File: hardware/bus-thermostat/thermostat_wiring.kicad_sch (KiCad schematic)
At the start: 44 parts, among them Q1 2N7002, Q2 2N7002, Q3 2N7002, Q4 IRF540N, Q5 IRF540N, T1 1:2, U1 UCC27714D

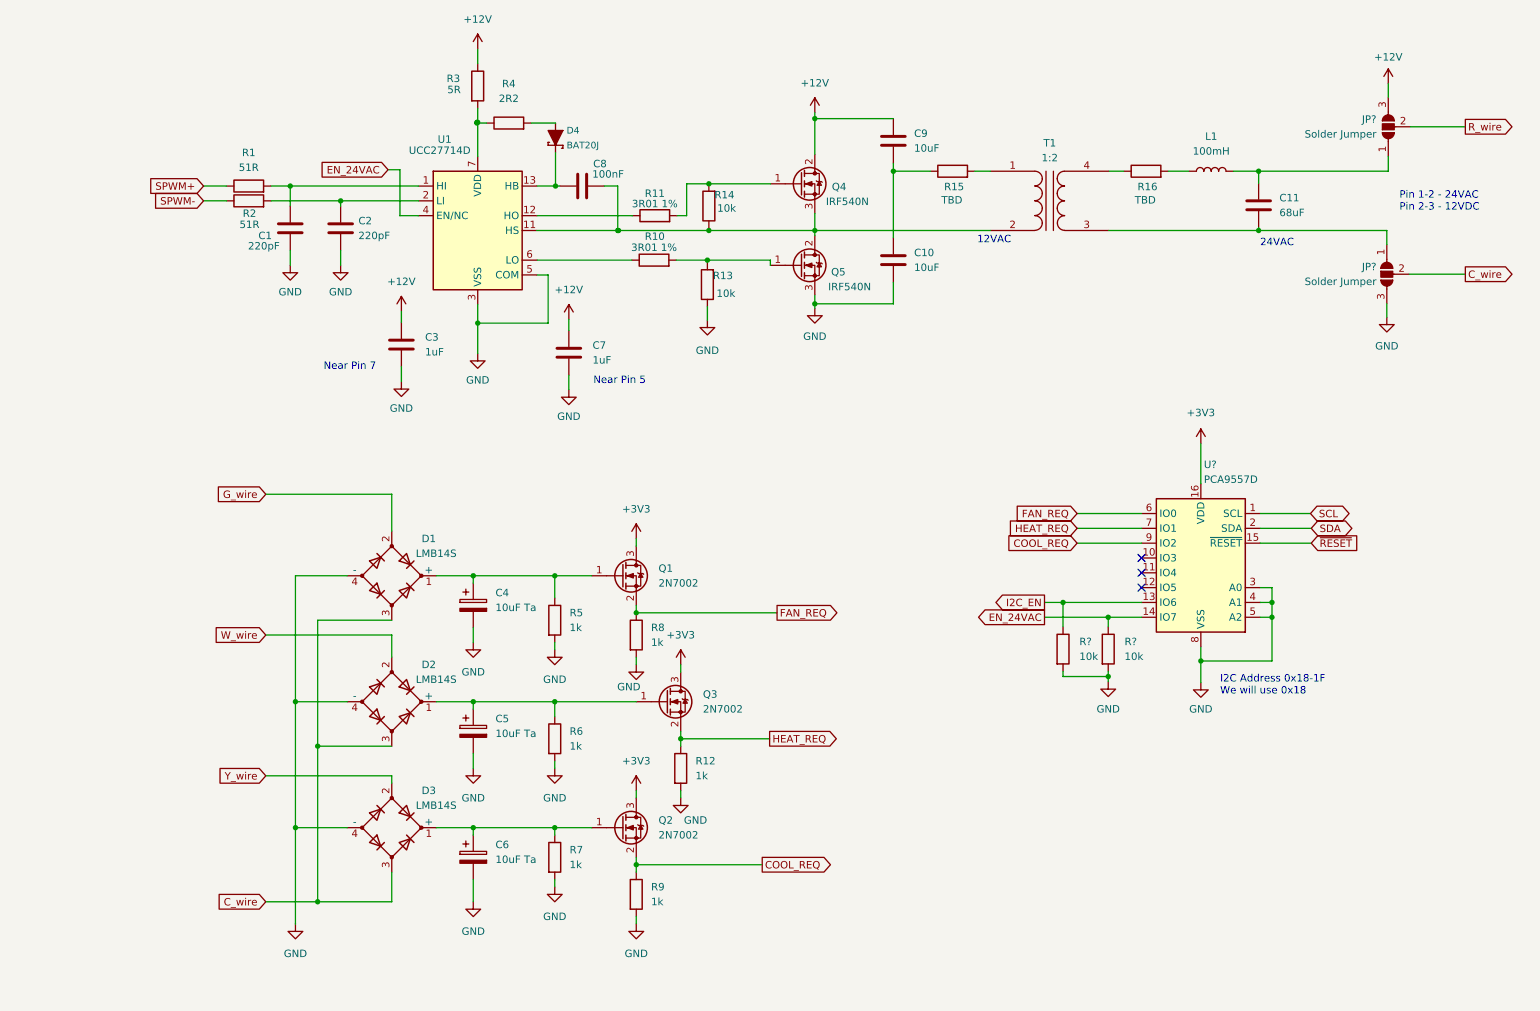
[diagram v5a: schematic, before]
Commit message: Rework the AC path generation again. Opamps only.
- awaiting the completion of analog circuit analysis
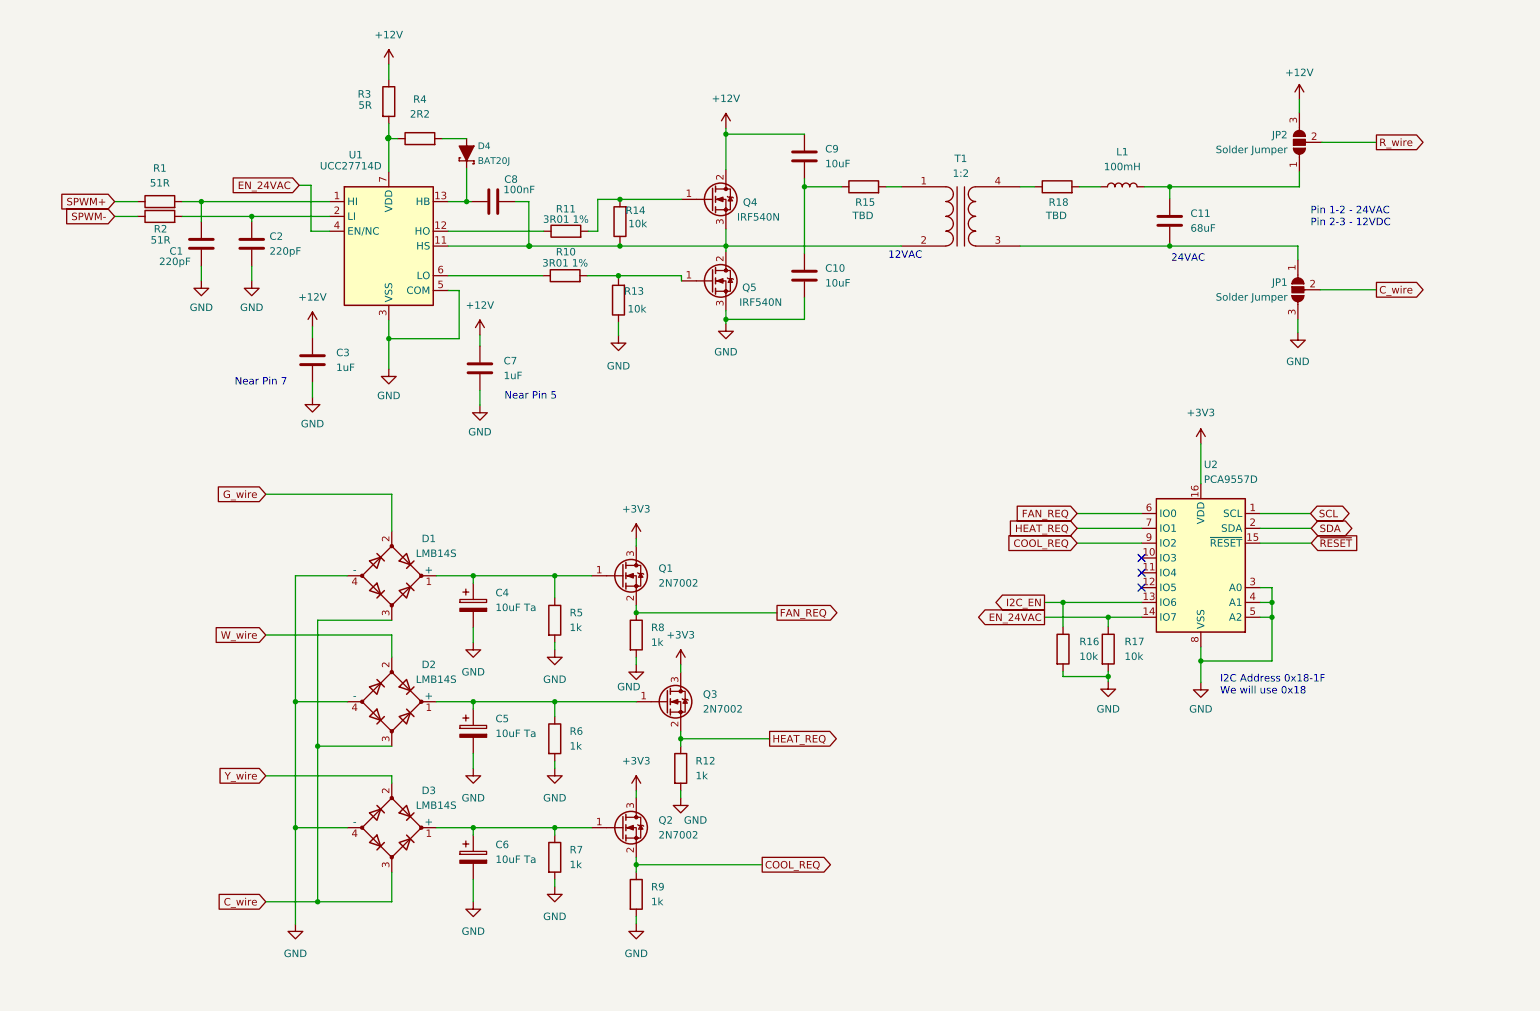
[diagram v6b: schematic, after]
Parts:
- gave numbers to parts that had none: 5
- renumbered R16 to R18
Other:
- moved on the sheet: C1, C10, C11, C2, C3, C7, C8, C9, D4, JP1, JP2, L1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

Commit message: Update some components
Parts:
- renumbered R18 to R16, R16 to R17, R17 to R18
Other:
- moved on the sheet: C4, C5, C6, D1, D2, D3, Q1, Q2, Q3, R12, R17, R18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

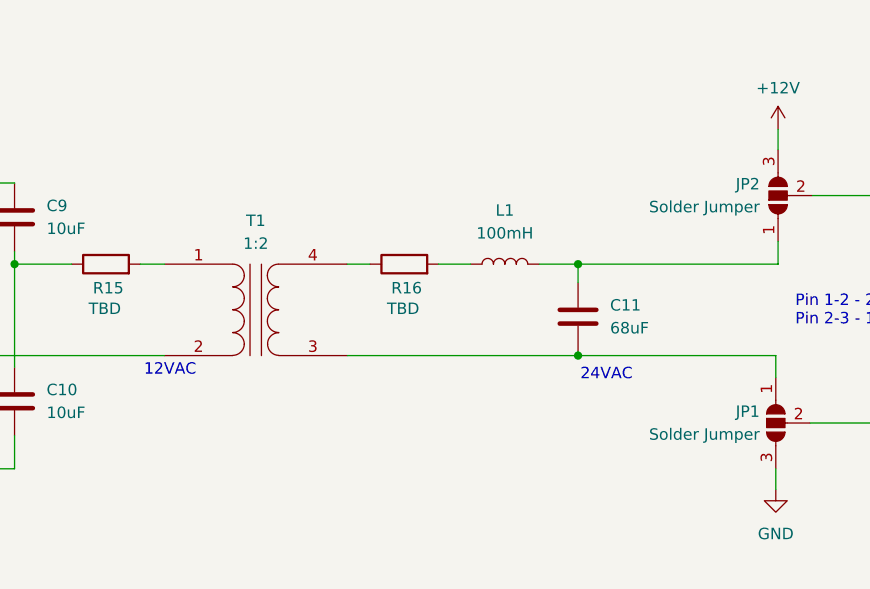
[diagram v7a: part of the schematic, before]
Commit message: Adjust PWMClock to 50kHz, use pulse transformers
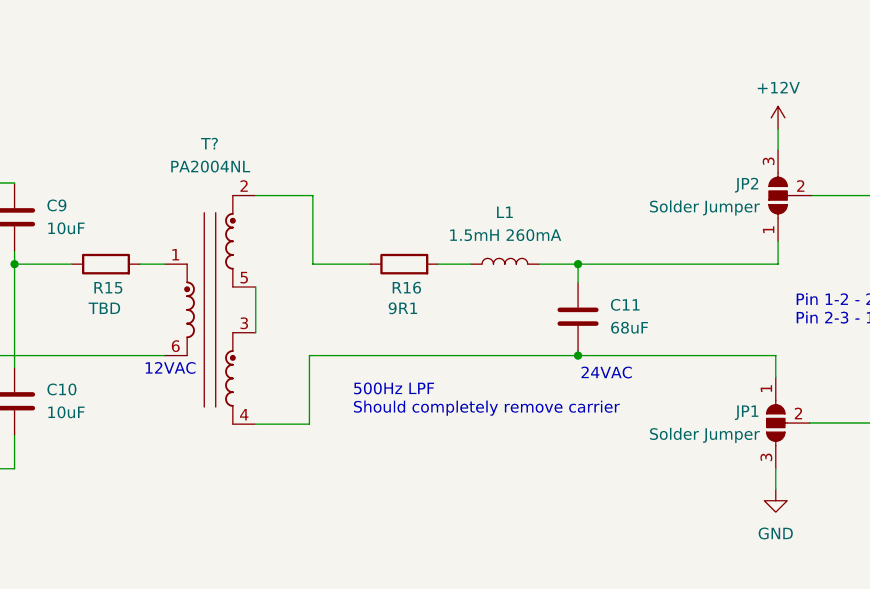
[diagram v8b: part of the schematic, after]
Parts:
- removed T1: 1:2, Transformer_THT:Transformer_Toroid_Horizontal_D9.0mm_Amidon-T30, symbol Device:Transformer_1P_1S
- added T?: PA2004NL, Transformer_SMD:Pulse_PA2004NL, symbol Transformer:PA2004NL
- L1: value 100mH -> 1.5mH 260mA; footprint (none) -> Inductor_THT:L_Radial_D28.0mm_P29.20mm
- R16: value TBD -> 9R1
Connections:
- net at Q4.3 (S), Q5.2 (D), R14.1: now also T?.6
- net at R15.2: now also T?.1
- net at C11.2, JP1.1 (A): now also T?.4
- net at R16.1: now also T?.2
- new net: T?.3, T?.5
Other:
- note added: "500Hz LPF Should completely remove carrier"
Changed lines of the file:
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@@
+    (stroke (width 0) (type default) (color 0 0 0 0))
+  )
+  (wire (pts (xy 189.103 64.135) (xy 195.072 64.135))
     (stroke (width 0) (type default) (color 0 0 0 0))
   )
@@
     (stroke (width 0) (type default) (color 0 0 0 0))
   )
+  (wire (pts (xy 195.072 64.135) (xy 195.072 56.515))
+    (stroke (width 0) (type default) (color 0 0 0 0))
+  )
   (wire (pts (xy 104.394 48.895) (xy 105.156 48.895))
     (stroke (width 0) (type default) (color 0 0 0 0))
@@
     (stroke (width 0) (type default) (color 0 0 0 0))
   )
+  (wire (pts (xy 189.103 48.895) (xy 189.103 53.975))
+    (stroke (width 0) (type default) (color 0 0 0 0))
+  )
   (wire (pts (xy 101.219 64.135) (xy 103.124 64.135))
     (stroke (width 0) (type default) (color 0 0 0 0))
@@
     (stroke (width 0) (type default) (color 0 0 0 0))
   )
-  (wire (pts (xy 199.263 46.355) (xy 201.803 46.355))
+  (wire (pts (xy 195.453 46.355) (xy 201.803 46.355))
     (stroke (width 0) (type default) (color 0 0 0 0))
   )
@@
     (stroke (width 0) (type default) (color 0 0 0 0))
   )
+  (wire (pts (xy 189.103 38.735) (xy 195.453 38.735))
+    (stroke (width 0) (type default) (color 0 0 0 0))
+  )
   (wire (pts (xy 58.928 48.895) (xy 80.899 48.895))
     (stroke (width 0) (type default) (color 0 0 0 0))
@@
     (stroke (width 0) (type default) (color 0 0 0 0))
   )
-  (wire (pts (xy 199.263 56.515) (xy 224.917 56.515))
-    (stroke (width 0) (type default) (color 0 0 0 0))
-  )
   (wire (pts (xy 249.936 130.048) (xy 249.936 127.508))
     (stroke (width 0) (type default) (color 0 0 0 0))
@@
     (stroke (width 0) (type default) (color 0 0 0 0))
   )
+  (wire (pts (xy 195.072 56.515) (xy 224.917 56.515))
+    (stroke (width 0) (type default) (color 0 0 0 0))
+  )
   (wire (pts (xy 249.936 140.081) (xy 249.936 132.588))
     (stroke (width 0) (type default) (color 0 0 0 0))
@@
   )
   (wire (pts (xy 72.136 175.387) (xy 72.136 170.307))
+    (stroke (width 0) (type default) (color 0 0 0 0))
+  )
+  (wire (pts (xy 195.453 38.735) (xy 195.453 46.355))
     (stroke (width 0) (type default) (color 0 0 0 0))
   )
@@
   )
   (text "Pin 1-2 - 24VAC\nPin 2-3 - 12VDC" (at 249.047 53.34 0)
+    (effects (font (size 1.27 1.27)) (justify left bottom))
+  )
+  (text "500Hz LPF\nShould completely remove carrier" (at 199.898 63.246 0)
     (effects (font (size 1.27 1.27)) (justify left bottom))
   )
@@
     (pin "2")
   )
+  (symbol (lib_id "Transformer:PA2004NL") (at 184.023 51.435 0) (unit 1)
+    (in_bom yes) (on_board yes) (fields_autoplaced)
+    (property "Reference" "T?" (id 0) (at 184.023 33.02 0))
+    (property "Value" "PA2004NL" (id 1) (at 184.023 35.56 0))
+    (property "Footprint" "Transformer_SMD:Pulse_PA2004NL" (id 2) (at 184.023 51.435 0)
+      (effects (font (size 1.27 1.27)) hide)
+    )
+    (property "Datasheet" "https://productfinder.pulseeng.com/products/datasheets/P663.pdf" (id 3) (at 176.403 51.435 0)
+      (effects (font (size 1.27 1.27)) hide)
+    )
+    (pin "1")
+    (pin "2")
+    (pin "3")
+    (pin "4")
+    (pin "5")
+    (pin "6")
+  )
   (symbol (lib_id "Transistor_FET:2N7002") (at 111.506 162.687 0) (unit 1)
     (in_bom yes) (on_board yes) (fields_autoplaced)
@@
     (pin "1")
     (pin "2")
-  )
-  (symbol (lib_id "Device:Transformer_1P_1S") (at 189.103 51.435 0) (unit 1)
-    (in_bom yes) (on_board yes) (fields_autoplaced)
-    (property "Reference" "T1" (id 0) (at 189.1157 41.529 0))
-    (property "Value" "1:2" (id 1) (at 189.1157 44.069 0))
-    (property "Footprint" "Transformer_THT:Transformer_Toroid_Horizontal_D9.0mm_Amidon-T30" (id 2) (at 189.103 51.435 0)
-      (effects (font (size 1.27 1.27)) hide)
-    )
-    (property "Datasheet" "~" (id 3) (at 189.103 51.435 0)
-      (effects (font (size 1.27 1.27)) hide)
-    )
-    (pin "1")
-    (pin "2")
-    (pin "3")
-    (pin "4")
   )
   (symbol (lib_id "power:GND") (at 114.046 134.747 0) (unit 1)
@@
   (symbol (lib_id "Device:L") (at 216.789 46.355 90) (unit 1)
     (in_bom yes) (on_board yes) (fields_autoplaced)
-    (property "Reference" "L1" (id 0) (at 216.789 40.386 90))
-    (property "Value" "100mH" (id 1) (at 216.789 42.926 90))
-    (property "Footprint" "" (id 2) (at 216.789 46.355 0)
+    (property "Reference" "L1" (id 0) (at 216.789 40.64 90))
+    (property "Value" "1.5mH 260mA" (id 1) (at 216.789 43.18 90))
+    (property "Footprint" "Inductor_THT:L_Radial_D28.0mm_P29.20mm" (id 2) (at 216.789 46.355 0)
       (effects (font (size 1.27 1.27)) hide)
     )
@@
     (in_bom yes) (on_board yes)
     (property "Reference" "R16" (id 0) (at 205.867 49.022 90))
-    (property "Value" "TBD" (id 1) (at 205.486 51.308 90))
+    (property "Value" "9R1" (id 1) (at 205.486 51.308 90))
     (property "Footprint" "" (id 2) (at 205.613 48.133 90)
       (effects (font (size 1.27 1.27)) hide)
